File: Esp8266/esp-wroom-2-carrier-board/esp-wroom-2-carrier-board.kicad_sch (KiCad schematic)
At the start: 18 parts, among them J1 DF9B-19S-1V69, J2 USB_B_Mini, Q1 MMBT2222A, Q2 MMBT2222A, U1 ESP-WROOM-02, U2 FT231XQ

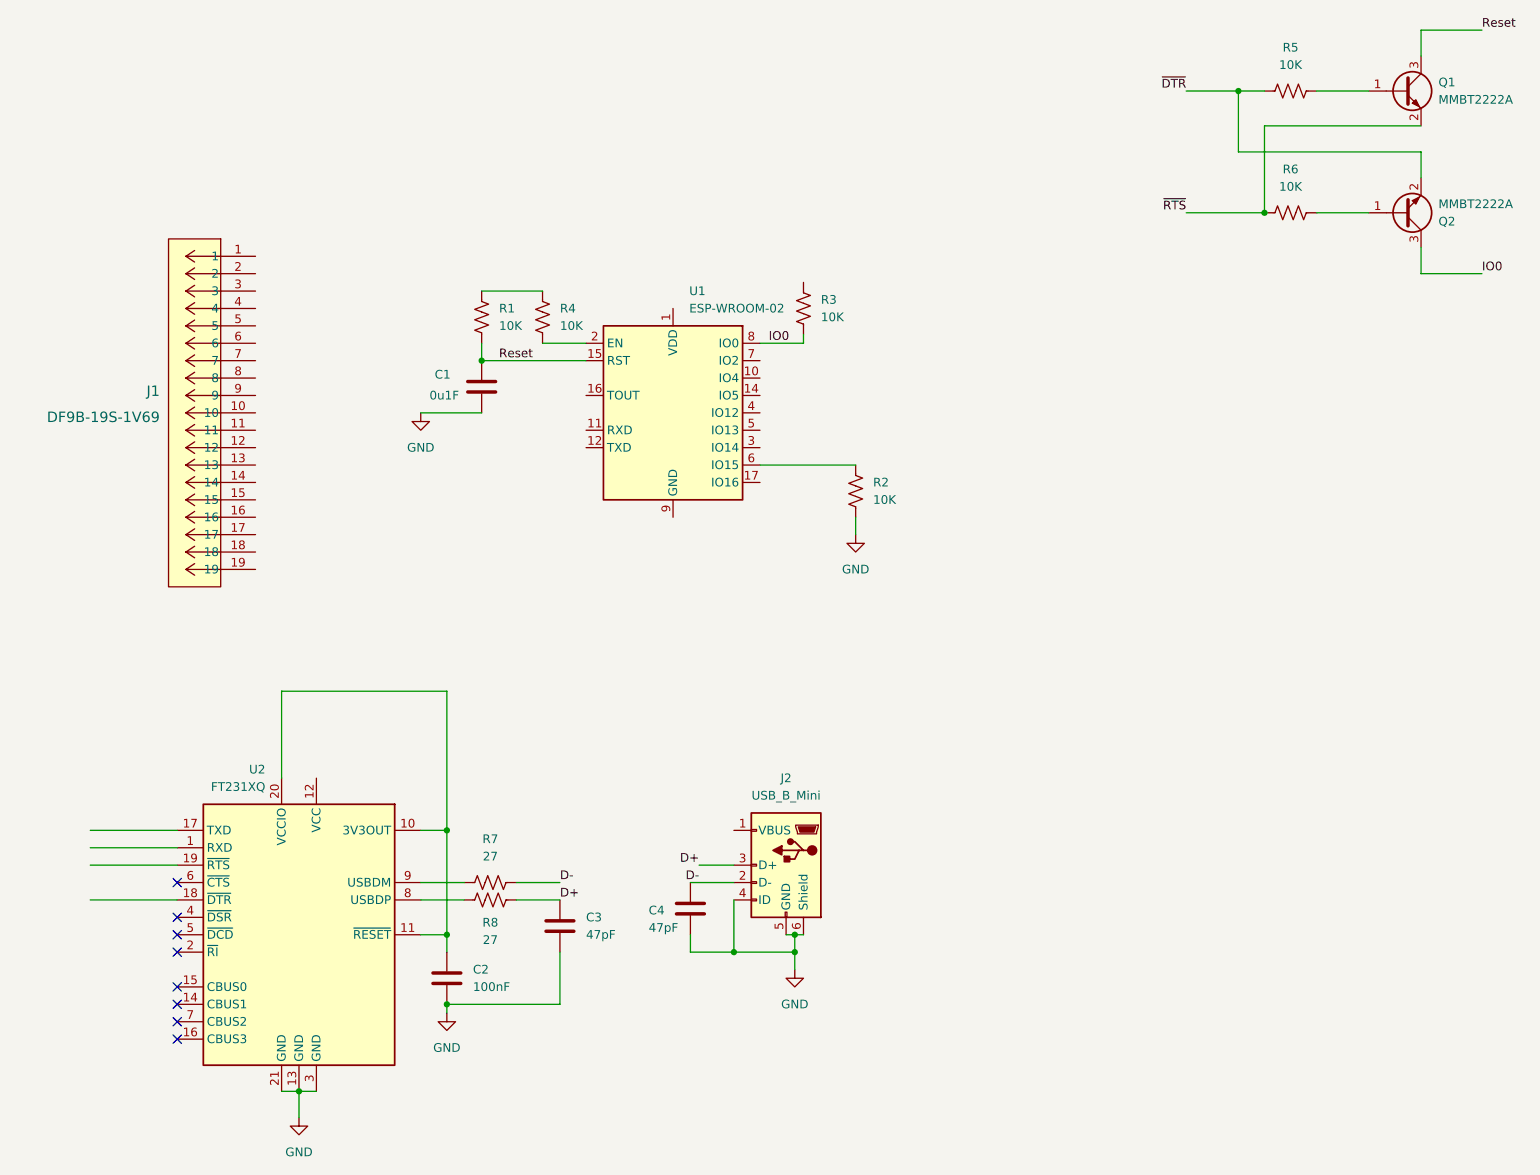
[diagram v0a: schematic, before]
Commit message: microcontroller
Wire micro controller pin out to connector
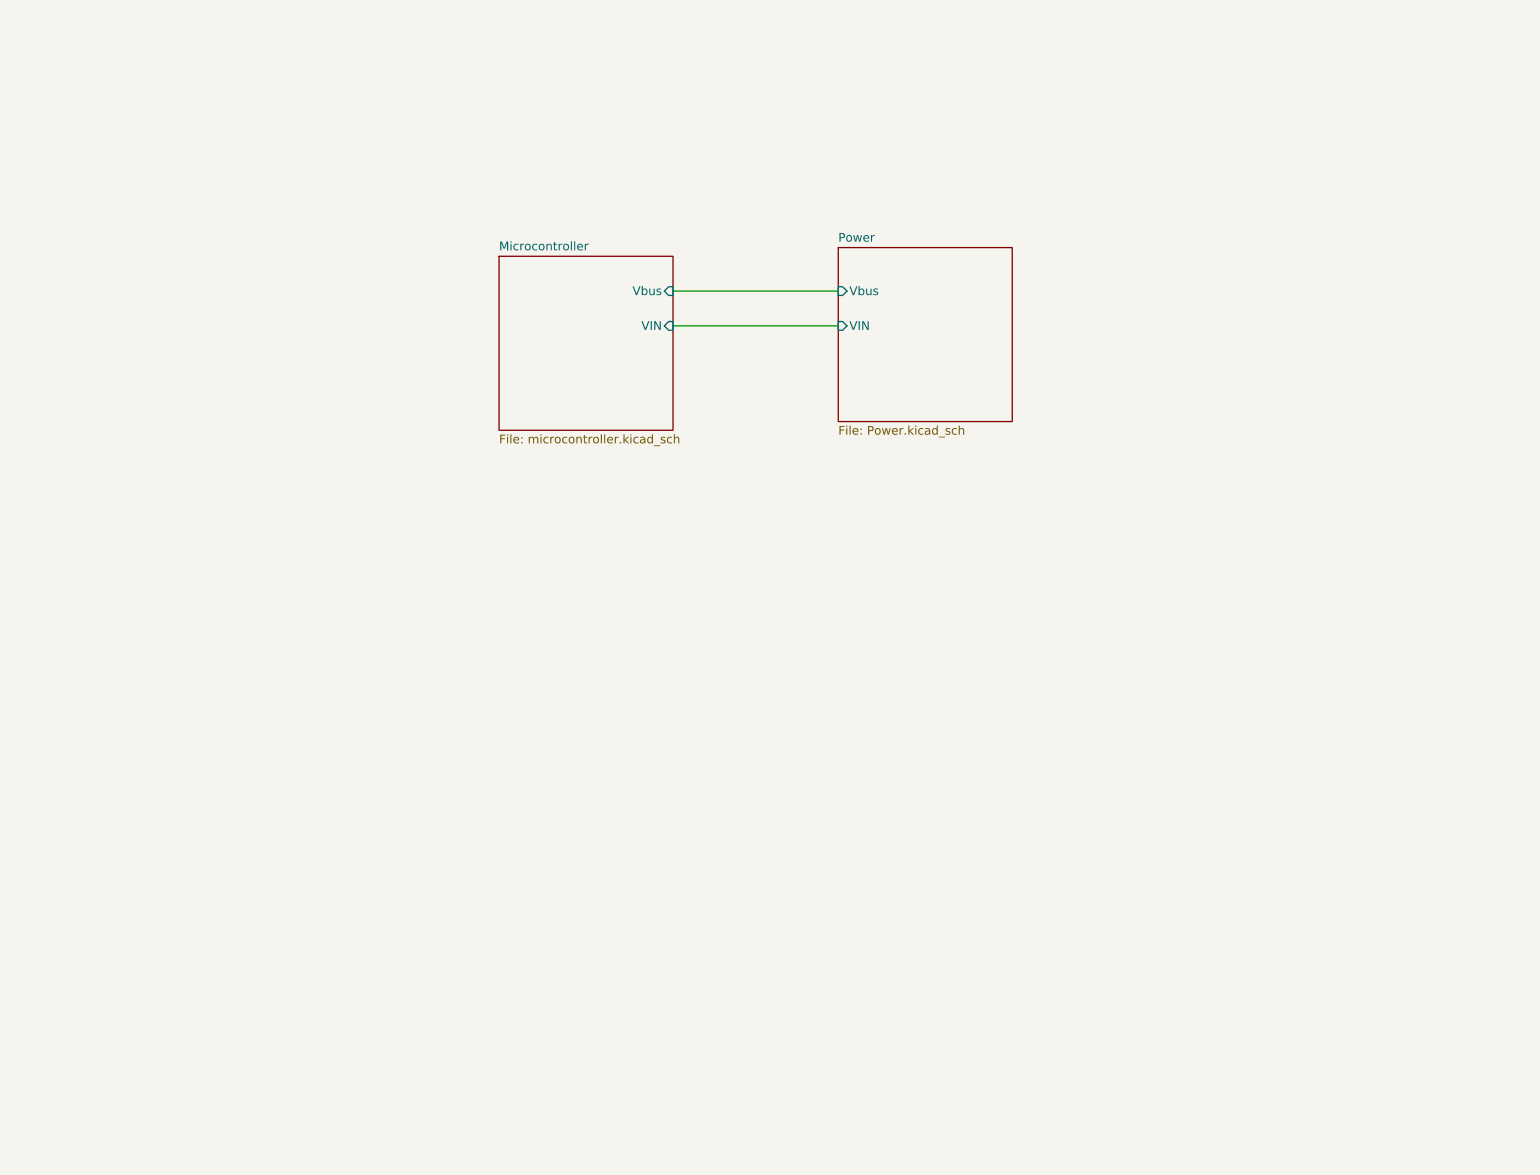
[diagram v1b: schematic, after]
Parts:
- removed C1: 0u1F, symbol Device:C
- removed C2: 100nF, symbol Device:C
- removed C3, C4: 47pF, symbol Device:C
- removed J1: DF9B-19S-1V69, User_Footprint:CON9_1X19_DL_DF9_HIR, symbol _Connectors:DF9B-19S-1V69
- removed J2: USB_B_Mini, symbol Connector:USB_B_Mini
- removed Q1, Q2: MMBT2222A, Package_TO_SOT_SMD:SOT-23, symbol Transistor_BJT:MMBT2222A
- removed R1, R2, R3, R4, R5, R6: 10K, Resistor_SMD:R_0805_2012Metric_Pad1.20x1.40mm_HandSolder, symbol Device:R_US
- removed R7, R8: 27, symbol Device:R_US
- removed U1: ESP-WROOM-02, RF_Module:ESP-WROOM-02, symbol RF_Module:ESP-WROOM-02
- removed U2: FT231XQ, Package_DFN_QFN:QFN-20-1EP_4x4mm_P0.5mm_EP2.5x2.5mm, symbol Interface_USB:FT231XQ
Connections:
- no-connect marks 8 -> 0
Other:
- added sheet Microcontroller (microcontroller.kicad_sch)
- added sheet Power (Power.kicad_sch)
